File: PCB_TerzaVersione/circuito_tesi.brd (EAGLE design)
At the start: 100 x 80 mm, 57 parts, among them IC1 SCD41-D-R2, J2 S5B-ZR-SM4A-TF_(LF)_(SN)CONN_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, Q1 BSS138, Q2 BSS138, Q3 BSS138, Q4 BSS138, U1 STMICROELECTRONICS_LIS3DHSTMI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, U3 MICS-6814, U6 BME280, Y1 ECS-.327-9-16-TR

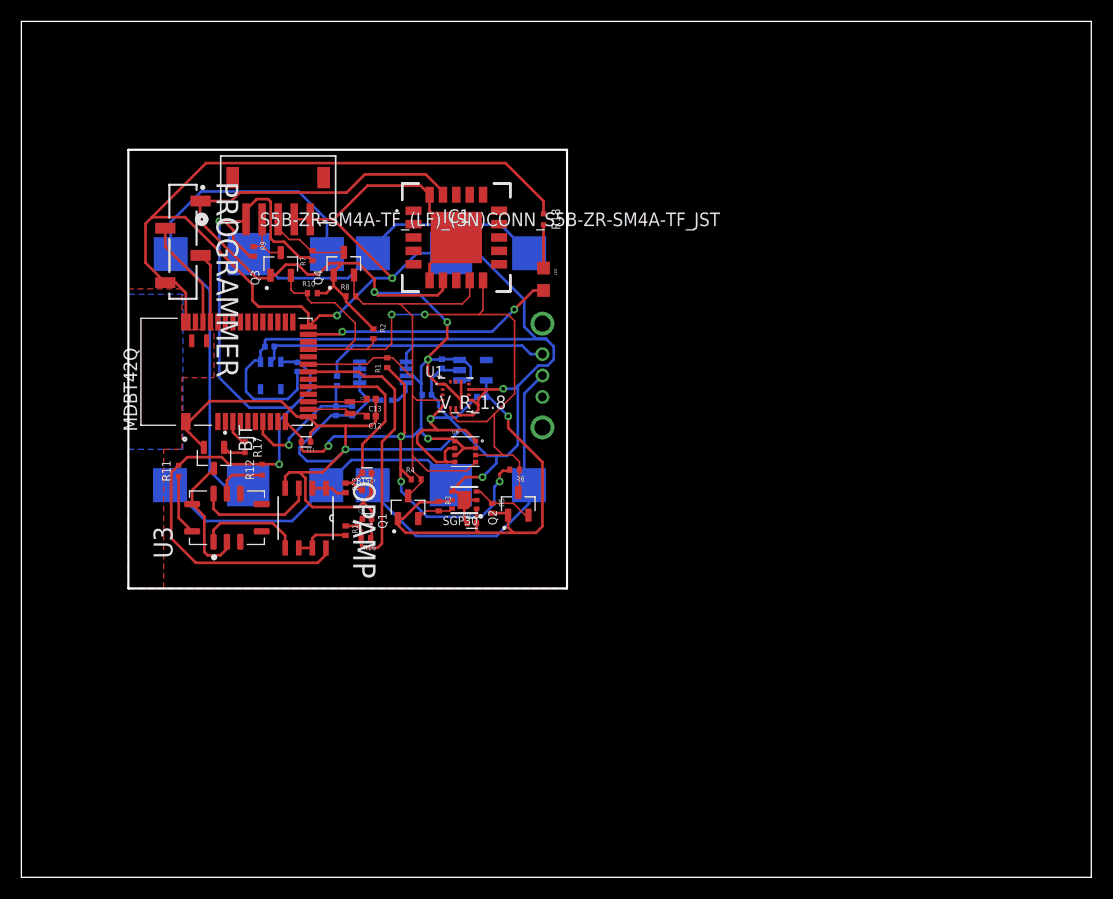
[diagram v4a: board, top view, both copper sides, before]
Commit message: Tolto resistenze pull up I2C
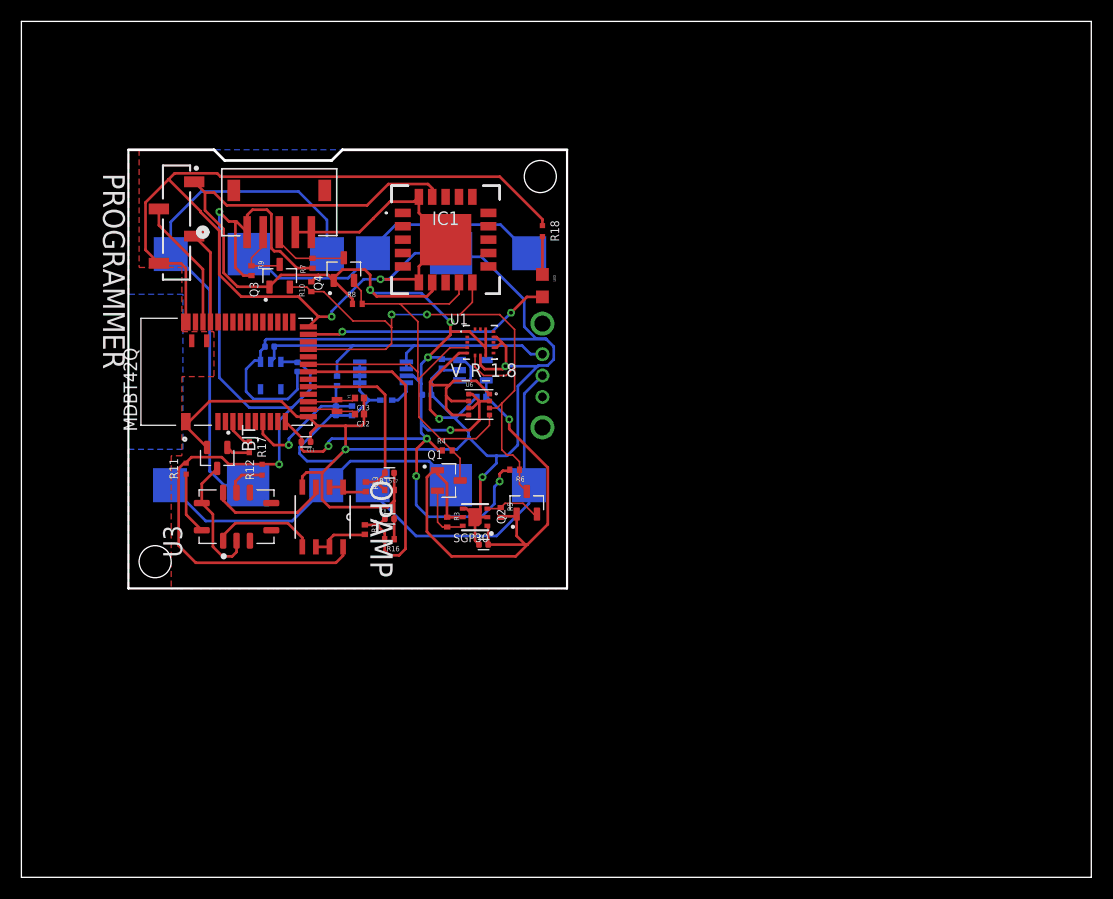
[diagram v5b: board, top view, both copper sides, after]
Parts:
- removed R1, R2: MCS0402MC1002FE000, Res_10K_0402:RESC1005X37N
- moved U1 5.41 mm to (42.9, 50.0)
- moved U6 4.59 mm to (42.8, 44.2)
- moved Q1 4.55 mm to (39.9, 37.1), turned to 0 degrees
- moved R4 3.96 mm to (39.8, 39.9)
- moved C10 2.28 mm to (43.2, 31.1)
- moved R16 2.20 mm to (34.4, 31.6)
- moved C7 2.10 mm to (34.4, 37.8)
- moved C8 2.10 mm to (34.4, 33.5)
- moved R15 2.10 mm to (34.4, 36.2)
- moved R13 1.90 mm to (32.2, 36.5)
- moved PROGRAMMER 1.90 mm to (14.5, 61.2)
- moved SGP30 1.89 mm to (42.4, 33.7)
- moved R9 1.81 mm to (21.5, 56.7)
- moved R14 1.80 mm to (32.1, 32.5)
- moved R3 1.70 mm to (39.8, 33.2)
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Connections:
- net 3.3V: no longer R1.1, R2.1
- net SCL: no longer R1.2
- net SDA: no longer R2.2
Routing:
- net 1.8V: track 42.2 -> 52.3 mm
- net 3.3V: track 152.4 -> 146.1 mm
- net SDA: track 65.6 -> 61.0 mm
- net 5V: track 88.0 -> 92.4 mm
- net AIN3: track 29.8 -> 32.0 mm
- net SWDCLK: track 6.61 -> 8.66 mm
- net SWDIO: track 10.2 -> 12.3 mm
- net SCL18: track 3.55 -> 5.54 mm
- net N$17: track 5.73 -> 4.55 mm
- net SDA5: track 5.34 -> 6.29 mm
- net N$11: track 4.74 -> 3.84 mm
- net SCL5: track 7.92 -> 8.66 mm
- net N$18: track 5.56 -> 4.85 mm
- net GND: track 330.6 -> 331.2 mm
- net AIN1: track 18.8 -> 18.3 mm
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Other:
- outline, holes or cut-outs redrawn

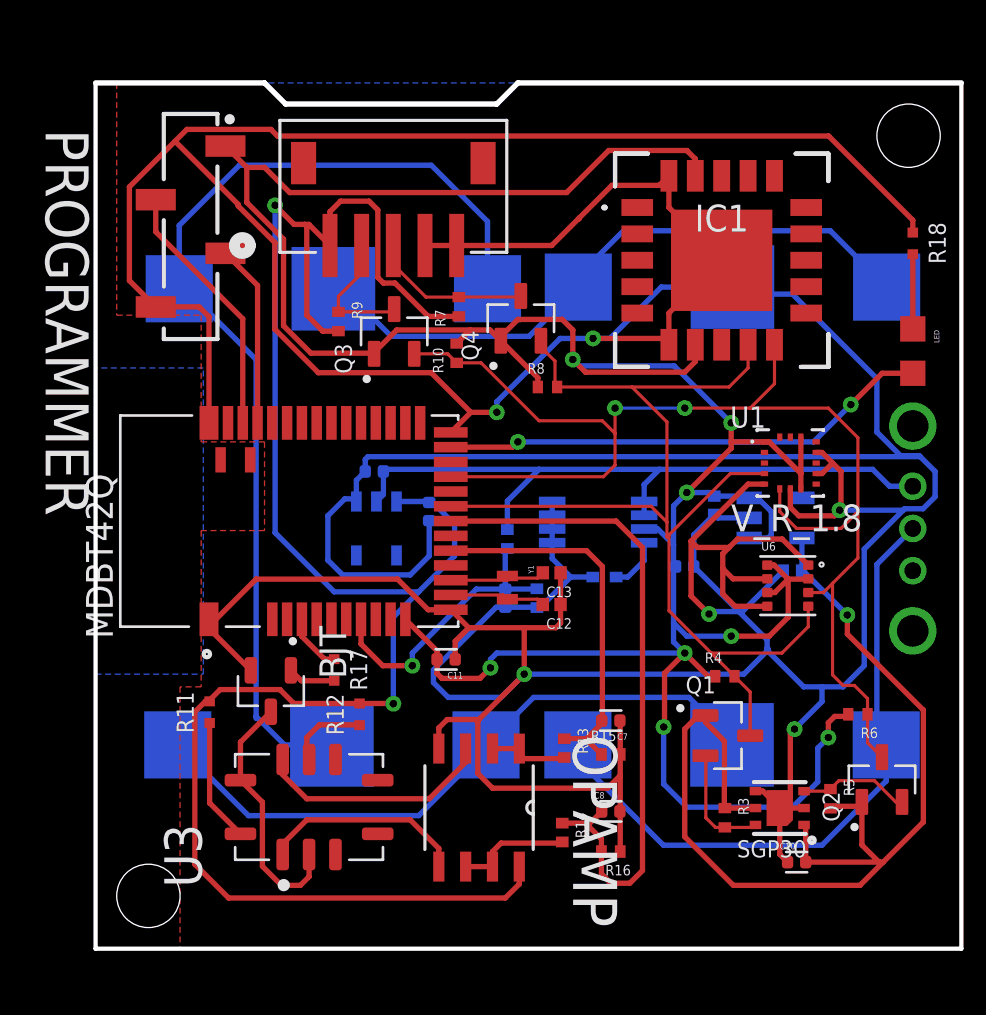
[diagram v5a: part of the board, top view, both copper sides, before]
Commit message: Aggiunto DRC
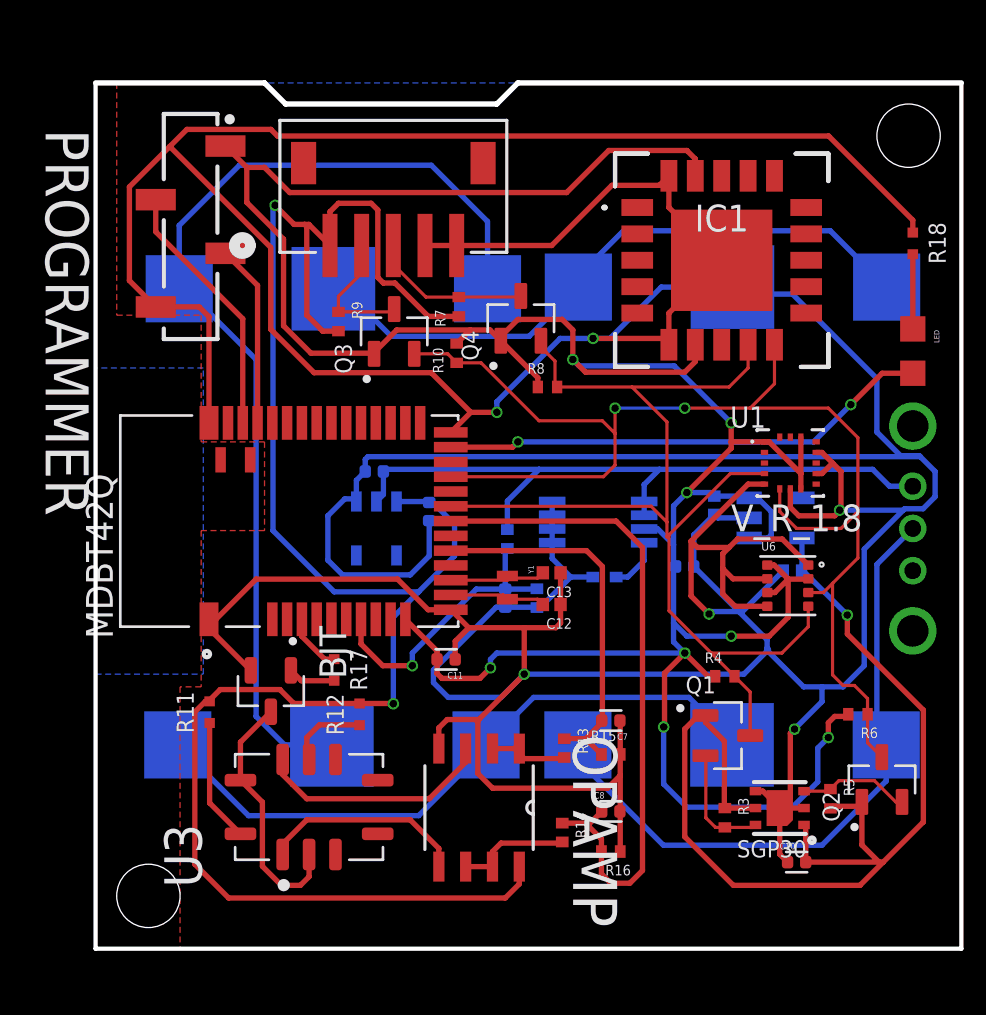
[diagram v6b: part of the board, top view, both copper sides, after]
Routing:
- net 3.3V: track 146.1 -> 144.8 mm
- net SCL5: track 8.66 -> 7.81 mm
- net GND: track 331.2 -> 330.7 mm

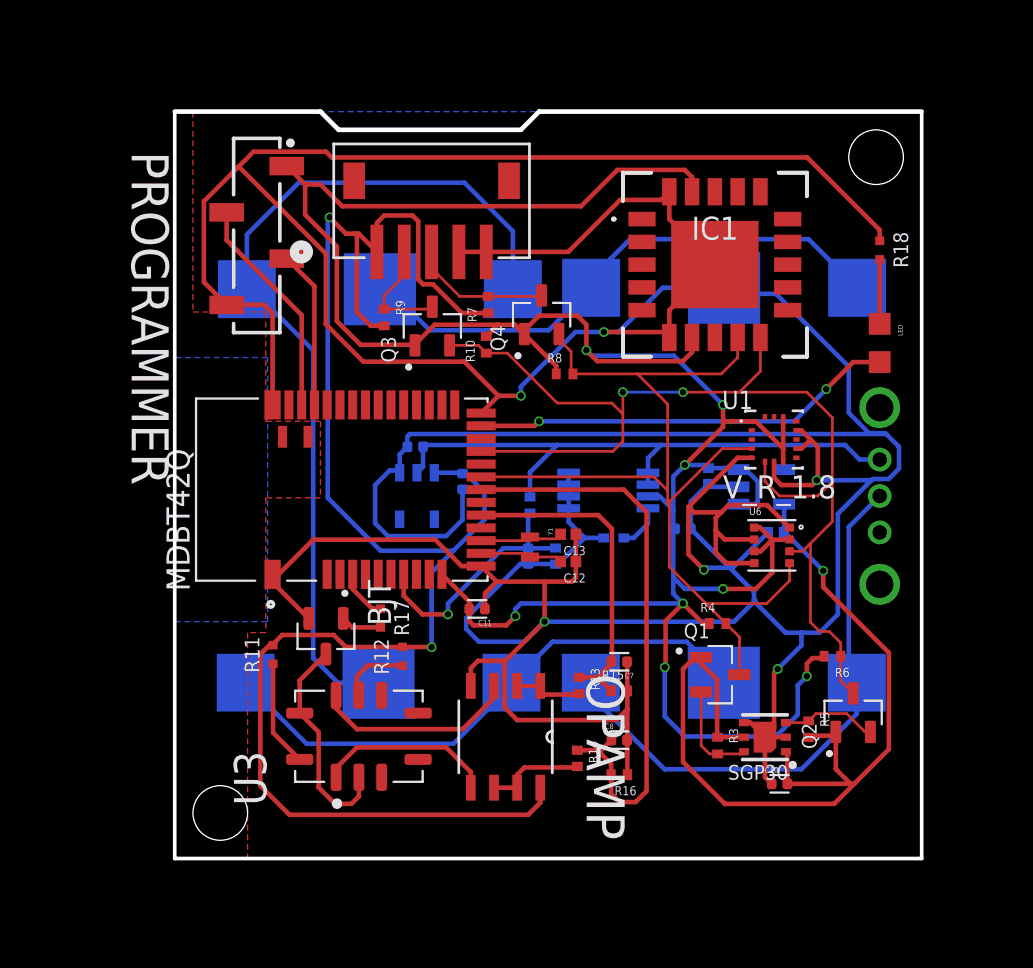
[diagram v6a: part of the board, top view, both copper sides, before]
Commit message: Sistemata posizione componenti
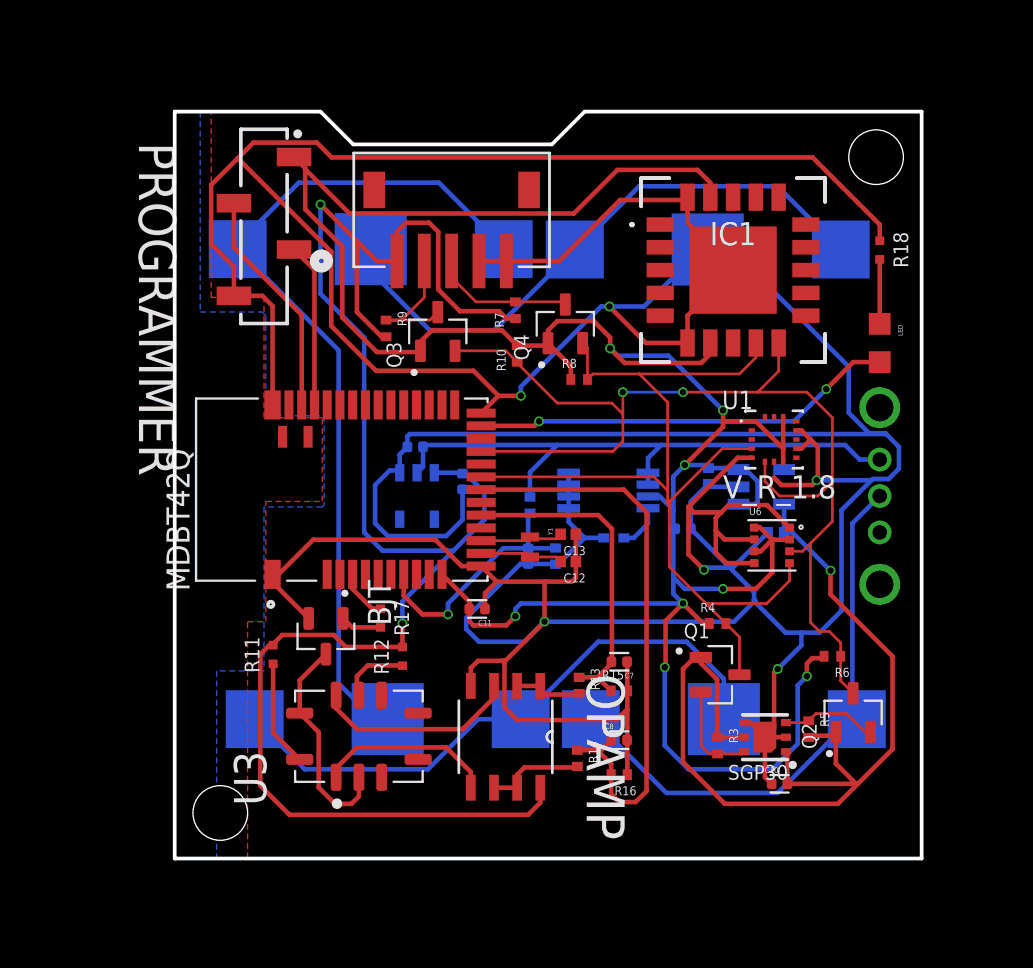
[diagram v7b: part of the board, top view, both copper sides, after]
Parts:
- moved BT4 2.28 mm to (39.3, 60.4)
- moved BT3 2.26 mm to (20.8, 60.5)
- moved BT2 2.06 mm to (21.7, 34.6)
- moved BT1 2.00 mm to (40.1, 34.6)
- moved R10 1.77 mm to (28.8, 54.7)
- moved R7 1.53 mm to (28.7, 57.1)
- moved Q4 1.39 mm to (31.4, 56.4)
- moved J2 1.21 mm to (22.2, 59.8)
- moved IC1 1.04 mm to (40.6, 59.3)
- moved R8 0.85 mm to (32.2, 53.3)
- moved PROGRAMMER 0.64 mm to (14.9, 61.7)
- moved R9 0.61 mm to (21.6, 56.1)
- moved Q3 0.42 mm to (24.4, 55.9)
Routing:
- net GND: track 330.7 -> 334.7 mm
- net 3.3V: track 144.8 -> 148.6 mm
- net N$25: track 30.7 -> 33.1 mm
- net 5V: track 92.4 -> 94.6 mm
- net N$2: track 31.1 -> 32.8 mm
- net N$4: track 49.1 -> 47.5 mm
- net SDA5: track 6.29 -> 7.63 mm
- net 1.8V: track 52.2 -> 53.0 mm
- net SDA: track 61.0 -> 60.3 mm
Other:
- outline, holes or cut-outs redrawn

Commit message: Aggiunti nomi
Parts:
- removed U3: MICS-6814, MICS-6814:SENSOR_MICS-6814
- removed U6: BME280, BME280:PSON65P250X250X100-8N
- added BME280: BME280, BME280:PSON65P250X250X100-8N
- added MICS6814: MICS-6814, MICS-6814:SENSOR_MICS-6814
- moved C7 0.70 mm to (34.4, 38.5)
- moved R11 0.70 mm to (16.1, 38.2)
- moved R15 0.41 mm to (34.5, 36.6)
- moved C9 0.40 mm to (29.0, 43.6)
- moved BJT 0.30 mm to (18.6, 39.2)
- moved R20 0.30 mm to (31.2, 43.6)
- moved C8 0.20 mm to (34.4, 33.7)
- moved R17 0.14 mm to (21.4, 40.3)
- renumbered IC1 to SCD41, J2 to SPS30, PROGRAMMER to PROG, U1 to LIS3DH, V_R_1.8 to VR_1.8, V_R_3.3 to VR_3.3, V_R_5 to VR_5, Y1 to CRYST
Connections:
- net 3.3V: now also BME280.2, BME280.6, BME280.8; no longer U6.2, U6.6, U6.8
- net BJT: now also MICS6814.B, MICS6814.J; no longer U3.B, U3.J
- net GND: now also BME280.1, BME280.5, BME280.7; no longer U6.1, U6.5, U6.7
- net N$10: now also MICS6814.H; no longer U3.H
- net N$11: now also MICS6814.G; no longer U3.G
- net N$13: now also MICS6814.K; no longer U3.K
- net N$6: now also MICS6814.A; no longer U3.A
- net SCL: now also BME280.4; no longer U6.4
- net SDA: now also BME280.3; no longer U6.3
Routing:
- net 5V: track 94.6 -> 92.8 mm
- net 3.3V: track 148.6 -> 149.6 mm
- net SDA: track 60.3 -> 59.3 mm
- net SCL: track 54.0 -> 54.9 mm
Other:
- board text added: "C"
- board text added: "C4"
- board text added: "D"
- board text added: "SPS30"
